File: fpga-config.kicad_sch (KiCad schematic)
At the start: 21 parts, among them J1 PinHeader_2x7_P2mm_SMD_Shroud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, Q1 BSS138PW, Q2 BSS138PW, Q3 BSS138PW, SW1 CVS-03B, SW2 SW_KMR211NGLFS_SMD, U2 TPD4E05U06QDQARQ1, U4 XC7K160T-FFG676

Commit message: [#57478] ohp release
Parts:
- D1, D2, D3: footprint sodimm-ddr5-tester-footprints:LED_0603_1608Metric_G -> antmicro-footprints:LED_0603_1608Metric_G; symbol sodimm-ddr5-tester:LED_G_0603_KP-1608CGCK -> antmicroLEDIndicationDiscrete:LED_G_0603_KP-1608CGCK
- J1: footprint sodimm-ddr5-tester-footprints:PinHeader_2x7_P2mm_SMD_Shrouded_no-locator -> antmicro-footprints:PinHeader_2x7_P2mm_SMD_Shrouded_no-locator; symbol sodimm-ddr5-tester:PinHeader_2x7_P2mm_SMD_Shrouded_no-locator -> antmicroGenericPinHeaders:PinHeader_2x7_P2mm_SMD_Shrouded_no-locator; now not fitted; now left out of the parts list
- Q1, Q2, Q3: footprint sodimm-ddr5-tester-footprints:SC70-3 -> antmicro-footprints:SC70-3; symbol sodimm-ddr5-tester:BSS138PW -> antmicroTransistorsFETsMOSFETsSingle:BSS138PW
- R11, R12, R13, R19: footprint sodimm-ddr5-tester-footprints:R_0402_1005Metric -> antmicro-footprints:R_0402_1005Metric; symbol sodimm-ddr5-tester:R_330R_0402 -> antmicroResistors0402:R_330R_0402
- R14, R15, R17: footprint sodimm-ddr5-tester-footprints:R_0402_1005Metric -> antmicro-footprints:R_0402_1005Metric; symbol sodimm-ddr5-tester:R_10k_0402 -> antmicroResistors0402:R_10k_0402
- R16, R18: footprint sodimm-ddr5-tester-footprints:R_0402_1005Metric -> antmicro-footprints:R_0402_1005Metric; symbol sodimm-ddr5-tester:R_4k7_0402 -> antmicroResistors0402:R_4k7_0402
- R20: footprint sodimm-ddr5-tester-footprints:R_0402_1005Metric_EIA -> antmicro-footprints:R_0402_1005Metric; symbol sodimm-ddr5-tester:R_0R_0402 -> antmicroResistors0402:R_0R_0402
- SW1: footprint sodimm-ddr5-tester-footprints:SW_DIP_SPSTx03_Slide_Copal_CVS-03xB_W5.9mm_P1mm -> antmicro-footprints:SW_DIP_SPSTx03_Slide_Copal_CVS-03xB_W5.9mm_P1mm; symbol sodimm-ddr5-tester:CVS-03B -> antmicroSlideSwitches:CVS-03B
- SW2: footprint sodimm-ddr5-tester-footprints:SW_KMR211NGLFS_SMD -> antmicro-footprints:SW_KMR211NGLFS_SMD; symbol sodimm-ddr5-tester:SW_KMR211NGLFS_SMD -> antmicroPushbuttonSwitches:SW_KMR211NGLFS_SMD
- U2: footprint sodimm-ddr5-tester-footprints:USON-10_2.5x1mm_P0.5mm -> antmicro-footprints:USON-10_2.5x1mm_P0.5mm; symbol sodimm-ddr5-tester:TPD4E05U06QDQARQ1 -> antmicroTVSDiodes:TPD4E05U06QDQARQ1; now not fitted; now left out of the parts list
- U4: footprint sodimm-ddr5-tester-footprints:BGA-676_27x27mm_Layout26x26_P1X1mm -> antmicro-footprints:BGA-676_27x27mm_Layout26x26_P1x1mm_FFG676; symbol sodimm-ddr5-tester:XC7K160T-FFG676 -> antmicroFPGAChips:XC7K160T-FFG676

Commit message: [#86301] Project refresh 81589
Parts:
- J1, U2: DNP DNP -> (none)

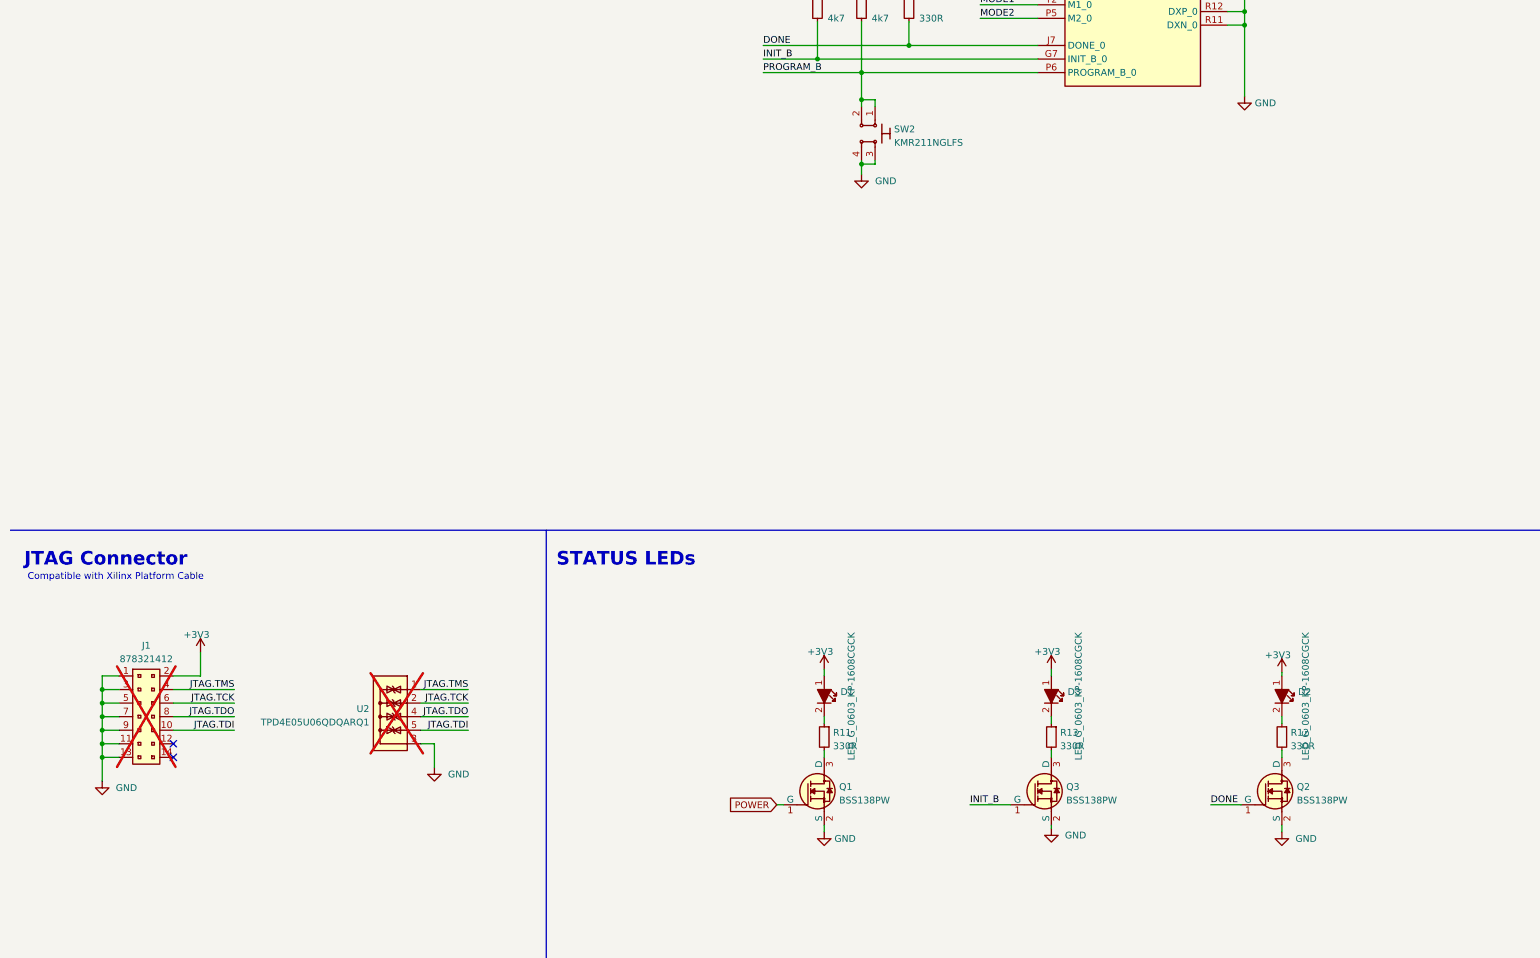
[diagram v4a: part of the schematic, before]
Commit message: [#87036] Update BSS138 transistors
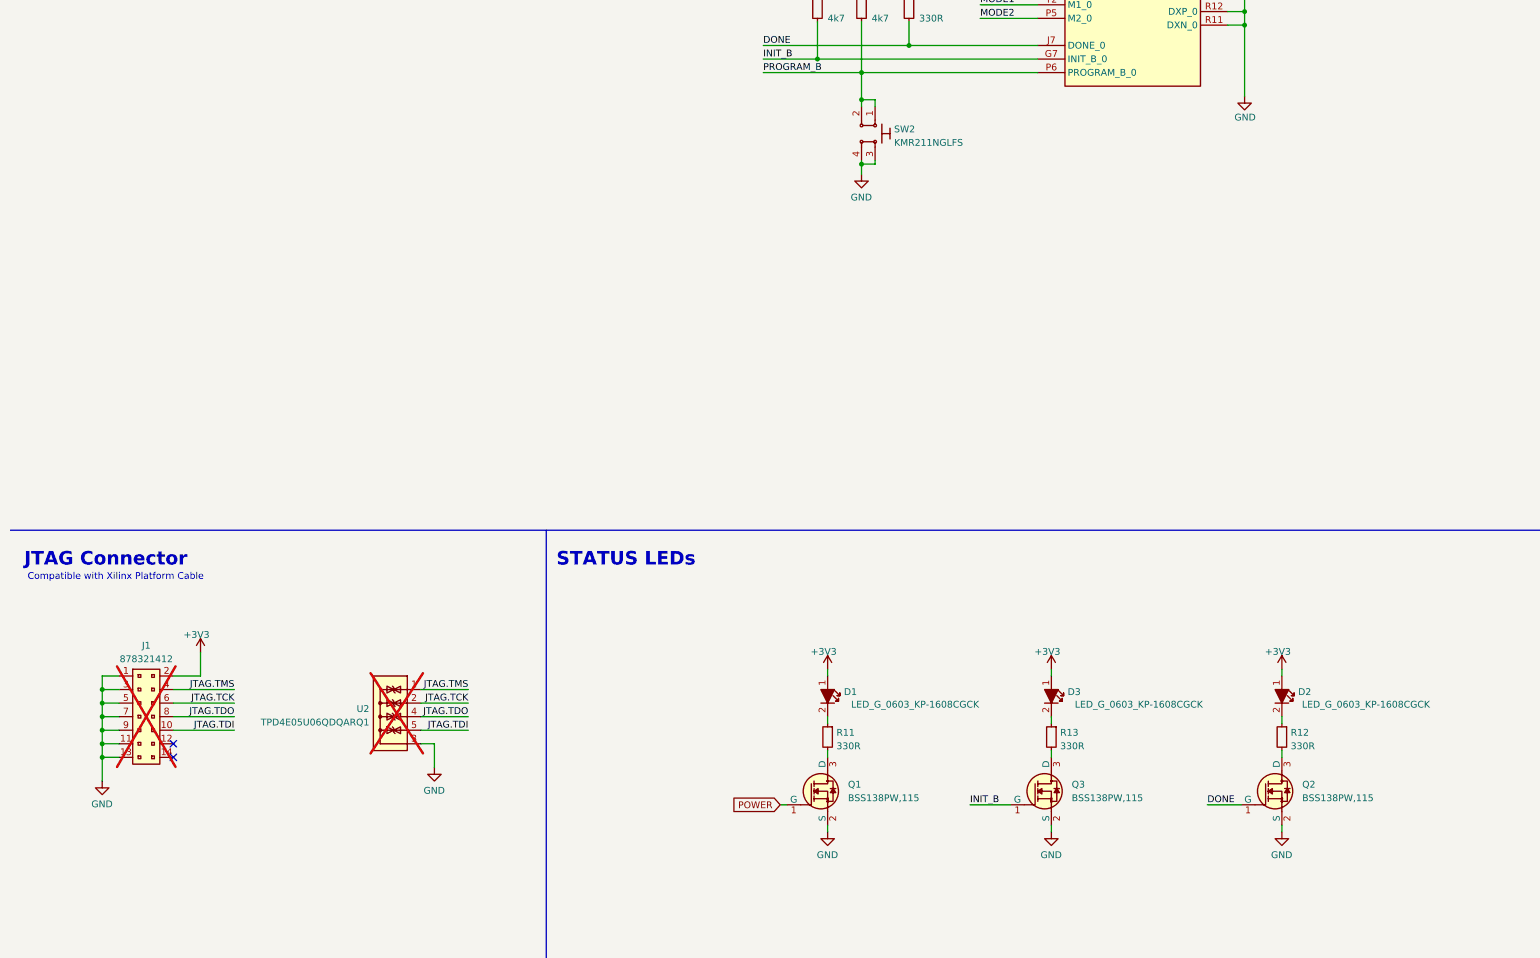
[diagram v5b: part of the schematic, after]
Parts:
- removed Q1, Q2, Q3: BSS138PW, antmicro-footprints:SC70-3, symbol antmicroTransistorsFETsMOSFETsSingle:BSS138PW
- added Q1, Q2, Q3: BSS138PW,115, antmicro-footprints:SC70-3, symbol antmicroTransistorsFETsMOSFETsSingle:BSS138PW,115
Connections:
- net DONE: now also Q2.1 (G)
- net GND: now also Q1.2 (S), Q2.2 (S), Q3.2 (S)
- net INIT_B: now also Q3.1 (G)
- net POWER: now also Q1.1 (G)
- net at R12.2: now also Q2.3 (D)
- net at R13.2: now also Q3.3 (D)
- net at R11.2: now also Q1.3 (D)
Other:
- moved on the sheet: D1, R11
